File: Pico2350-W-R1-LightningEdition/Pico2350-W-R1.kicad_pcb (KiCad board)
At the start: 4 copper layers, 21 x 58 mm, 71 parts, among them J1 USB_C_Receptacle_USB2.0_16P, J2 Conn_01x20, J3 Conn_01x20, J4 Conn_01x03, SW1 SW_Push, U1 RP2350_60QFN, U2 ZD25WQ32CEIGR, U3 MIC5205-3.3YM5, U4 ESP8685H4, U5 ADXL345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

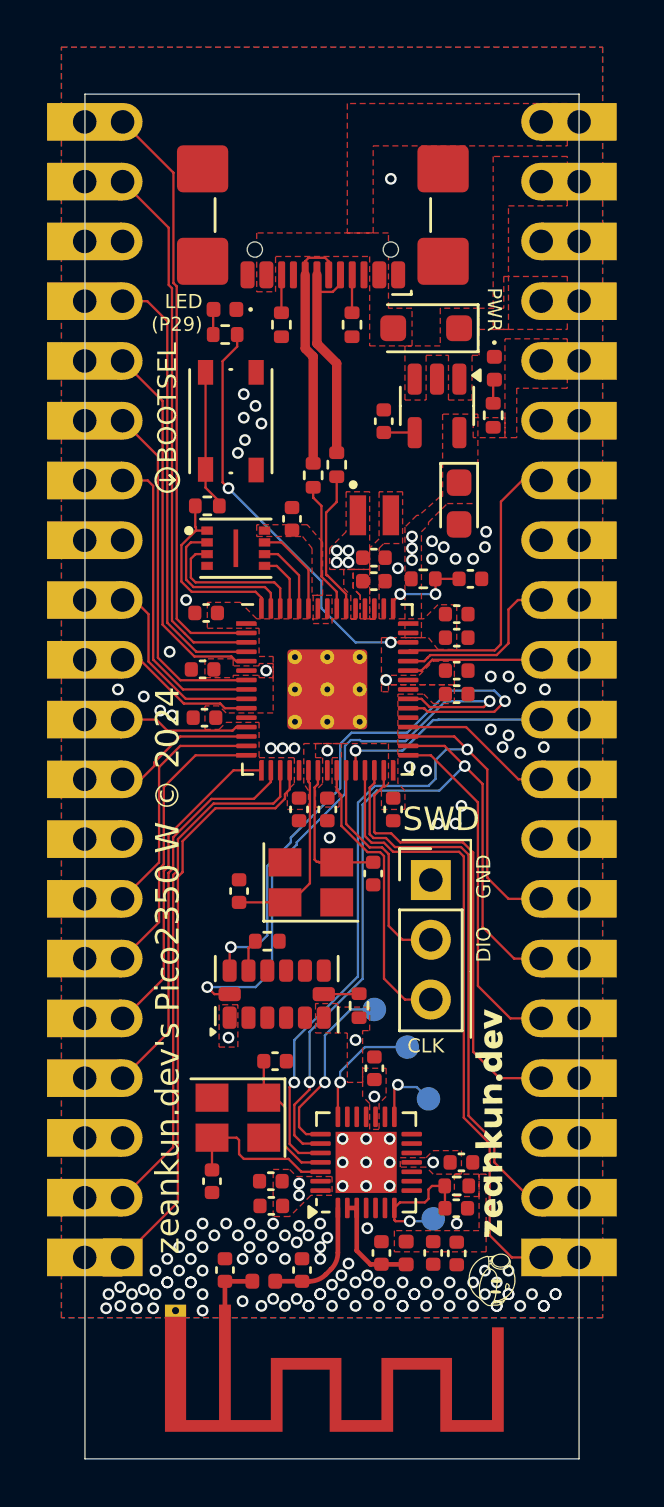
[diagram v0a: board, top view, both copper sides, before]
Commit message: fix disconnection because of stitching vias that retards ask for repetitively
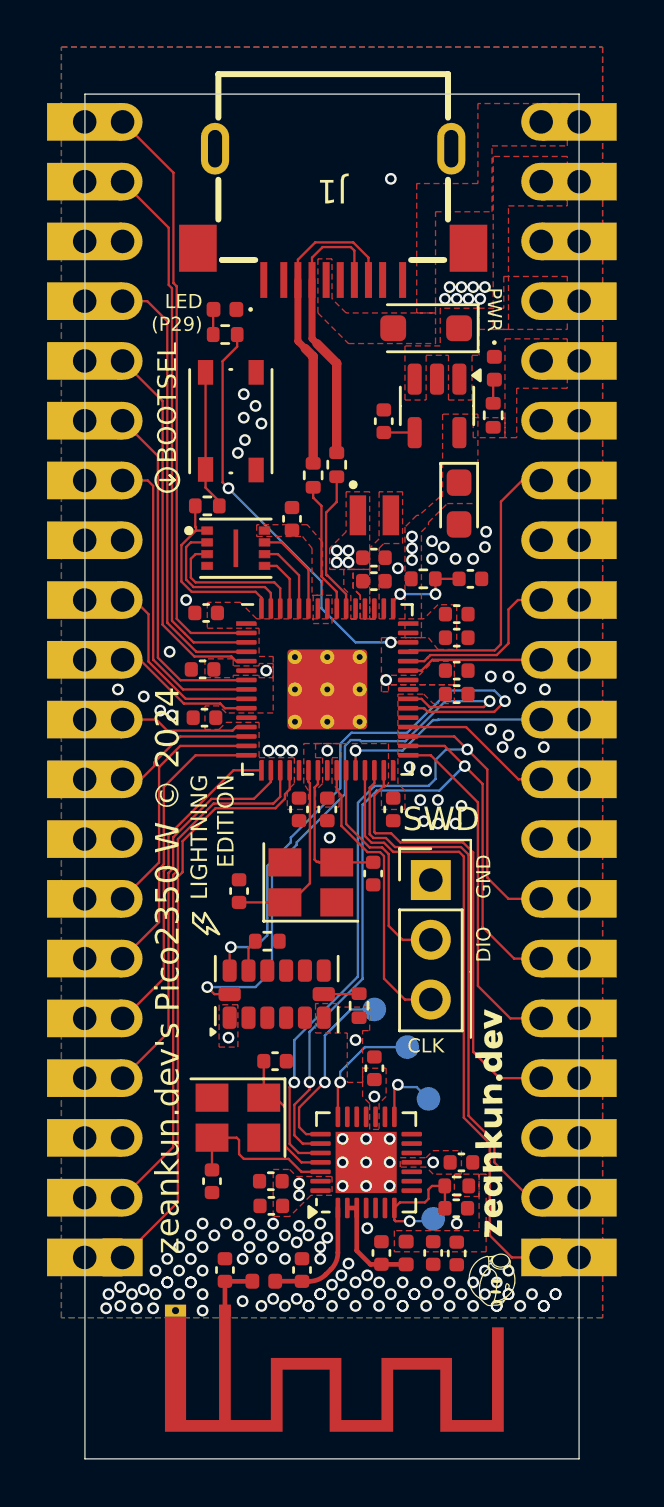
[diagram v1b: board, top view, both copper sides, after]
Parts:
- removed R4, R5: 5.1k, Resistor_SMD:R_0402_1005Metric
- J1: value USB_C_Receptacle_USB2.0_16P -> USB_Lightning_Apple; footprint Connector_USB:USB_C_Receptacle_GCT_USB4110 -> RP2350_60QFN_minimal:Apple_LightningConnector_ShouHan
- moved J1 0.55 mm to (80.5, 33.6)
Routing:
- net /USB_DP: track 10.4 -> 13.4 mm
- net /USB_DM: track 10.1 -> 12.0 mm
- net Net-(J1-CC2): track 1.61 -> 0.00 mm
- net Net-(J1-CC1): track 1.61 -> 0.00 mm
- net GND: vias 139 -> 150
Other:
- board text added: "Apple(R) Lightning is a trademark of Apple Inc. All rights reserved."
- board text added: "LIGHTNING EDITION"
- board text added: "NOT A {dblquote}MADE FOR IPHONE{dblquote} DEVICE MACS MAY NOT BE SUPPORTED"
- board text added: "Uses ESP8685H2 by Espressif."
- board text added: "for the sake of tim cook"
- board text removed: "Uses ESP8685H2 by Espressif Systems."
